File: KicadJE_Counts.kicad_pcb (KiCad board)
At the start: 2 copper layers, 242 x 128 mm, 215 parts, among them J108 Conn_02x03_Male, J201 ClockOut, J202 ClockIn, J203 Out0, J204 Out1, J205 Out2, J206 Out3, J207 Out4, J208 Out5, J209 Out6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

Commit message: Update KicadJE_Counts.kicad_pcb
input circuit
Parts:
- moved R331 103.4 mm to (45.4, 106.1)
- moved C321 97.8 mm to (45.2, 110.0)
- moved R304 76.0 mm to (85.8, 112.0)
- moved R303 72.9 mm to (82.0, 112.0)
- moved R301 67.6 mm to (58.0, 112.0), turned to 180 degrees
- moved R302 64.7 mm to (54.2, 112.0), turned to 180 degrees
- moved D314 56.9 mm to (44.8, 99.5)
- moved D313 56.9 mm to (44.9, 101.8)
- moved D307 44.8 mm to (42.5, 119.2)
- moved D308 44.8 mm to (42.7, 117.1)
- moved C313 7.06 mm to (62.0, 112.0), turned to 180 degrees
- moved C314 6.74 mm to (78.0, 112.0), turned to 0 degrees
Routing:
- net Net-(C314-Pad1): track 0.00 -> 40.0 mm
- net Net-(C313-Pad1): track 0.00 -> 21.0 mm
- net -12V: track 90.7 -> 93.2 mm
- net +12V: track 141.7 -> 144.2 mm
- net Net-(C314-Pad2): track 0.00 -> 2.45 mm
- net Net-(C313-Pad2): track 0.00 -> 1.98 mm
- net In_2: track 0.00 -> 1.70 mm
- net In_1: track 0.00 -> 1.68 mm

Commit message: Update KicadJE_Counts.kicad_pcb
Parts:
- moved R313 126.6 mm to (84.5, 62.5), turned to 180 degrees
- moved C315 116.8 mm to (75.2, 67.8), turned to 270 degrees
- moved R320 112.3 mm to (78.0, 85.0), turned to 180 degrees
- moved R326 111.7 mm to (81.8, 85.0), turned to 180 degrees
- moved R315 111.5 mm to (63.8, 63.2), turned to 270 degrees
- moved R306 111.4 mm to (75.2, 64.0), turned to 90 degrees
- moved R314 110.4 mm to (84.5, 65.0), turned to 180 degrees
- moved R319 104.3 mm to (56.0, 87.5)
- moved R316 104.0 mm to (63.8, 67.0), turned to 270 degrees
- moved D309 96.9 mm to (55.2, 65.0), turned to 270 degrees
- moved D310 94.0 mm to (57.5, 65.0), turned to 90 degrees
- moved R328 86.6 mm to (56.0, 85.0)
- moved R321 76.6 mm to (80.0, 94.0), turned to 180 degrees
- moved D307 64.4 mm to (77.2, 65.0), turned to 90 degrees
- moved D308 63.8 mm to (79.5, 65.0), turned to 270 degrees
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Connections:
- R313 pad 1: (no net) -> /KicadJE_Counts2/POT3_L
- RV303 pad 1: (no net) -> /KicadJE_Counts2/POT3_L

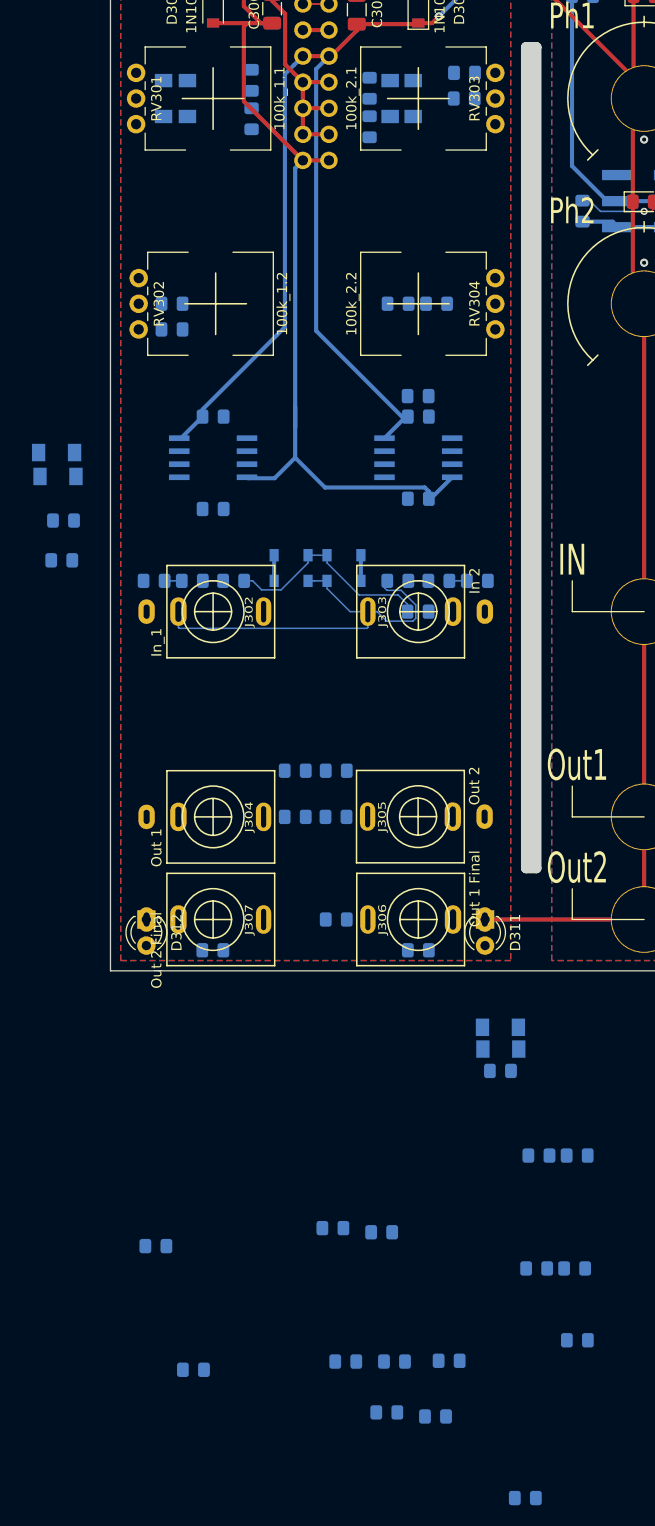
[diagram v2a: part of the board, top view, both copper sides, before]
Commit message: Changed label types for POT's
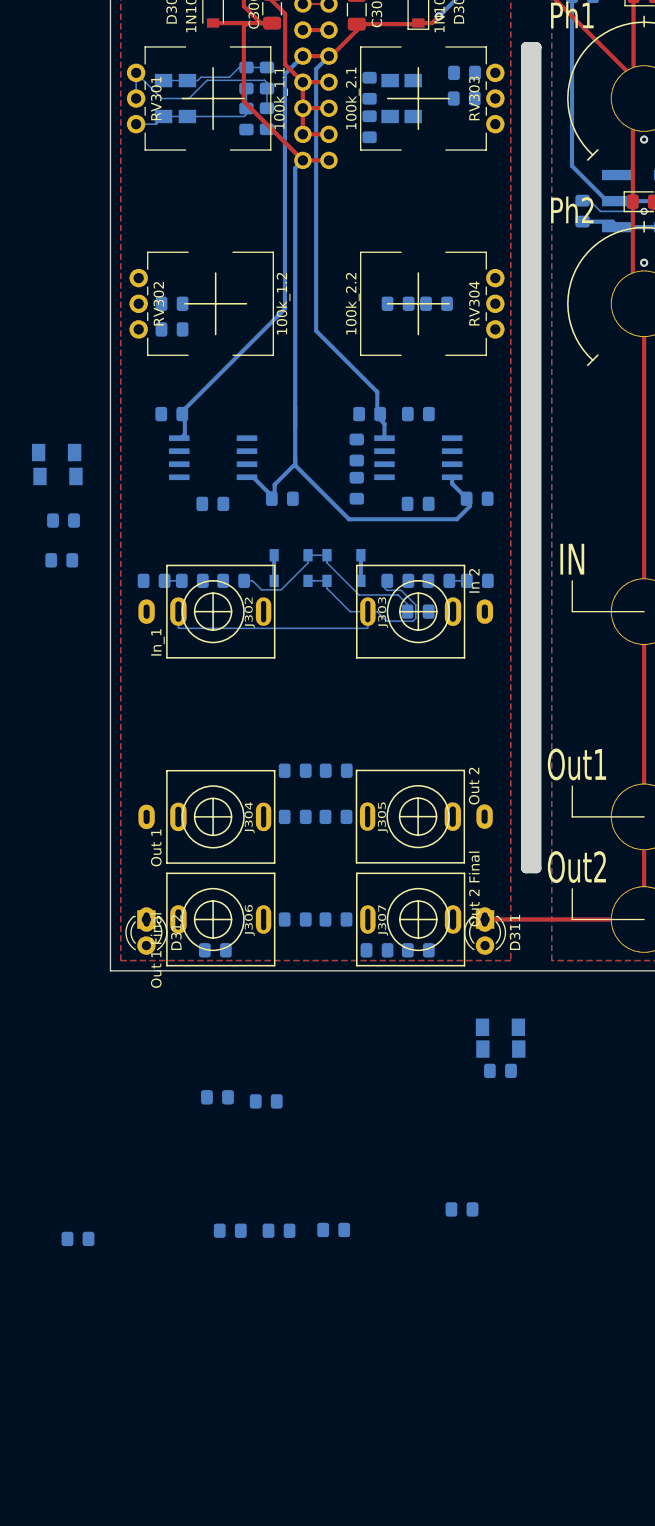
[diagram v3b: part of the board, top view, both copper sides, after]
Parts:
- moved C320 119.4 mm to (63.2, 63.0), turned to 90 degrees
- moved R307 116.5 mm to (63.2, 67.0), turned to 270 degrees
- moved R323 101.5 mm to (60.0, 104.5), turned to 180 degrees
- moved R322 88.9 mm to (80.0, 104.5), turned to 180 degrees
- moved R308 71.0 mm to (74.0, 99.2), turned to 90 degrees
- moved R311 68.5 mm to (74.0, 103.0), turned to 90 degrees
- moved R330 45.0 mm to (76.0, 148.0)
- moved C319 36.3 mm to (72.0, 145.0), turned to 180 degrees
- moved J306 20.0 mm to (60.0, 145.0), turned to 270 degrees
- moved J307 20.0 mm to (80.0, 145.0), turned to 90 degrees
- moved R309 17.0 mm to (71.8, 175.2)
- moved R310 17.0 mm to (46.8, 176.1)
- moved R312 17.0 mm to (84.2, 173.2)
- moved R324 17.0 mm to (65.2, 162.7)
- moved R325 17.0 mm to (66.4, 175.3)
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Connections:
- net /KicadJE_Counts2/POT1_L renamed POT1_L
- R315 pad 2: /KicadJE_Counts2/POT1_C -> POT1_C
- R316 pad 1: /KicadJE_Counts2/POT1_C -> POT1_C
- RV301 pad 2: /KicadJE_Counts2/POT1_C -> POT1_C
- RV301 pad 3: (no net) -> POT1_C
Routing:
- net POT1_C: track 0.00 -> 19.6 mm
- net POT1_L: track 0.00 -> 14.8 mm
- net Net-(C320-Pad2): track 0.00 -> 10.6 mm
- net -12V: track 93.2 -> 101.1 mm
- net +12V: track 144.2 -> 141.9 mm

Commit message: Update KicadJE_Counts.kicad_pcb
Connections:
- net /KicadJE_Counts2/POT2_L renamed POT2_L
- net /KicadJE_Counts2/POT3_L renamed POT3_L
- net /KicadJE_Counts2/POT4_L renamed POT4_L
- R314 pad 1: /KicadJE_Counts2/POT3_C -> POT3_C
- R317 pad 1: /KicadJE_Counts2/POT3_C -> POT3_C
- R322 pad 2: /KicadJE_Counts2/POT3_C -> POT3_C
- R327 pad 2: /KicadJE_Counts2/POT4_C -> POT4_C
- R328 pad 1: /KicadJE_Counts2/POT2_C -> POT2_C
- R330 pad 2: /KicadJE_Counts2/POT4_C -> POT4_C
- RV302 pad 2: /KicadJE_Counts2/POT2_C -> POT2_C
- RV302 pad 3: (no net) -> POT2_C
- RV303 pad 2: /KicadJE_Counts2/POT3_C -> POT3_C
- RV303 pad 3: (no net) -> POT3_C
- RV304 pad 2: /KicadJE_Counts2/POT4_C -> POT4_C
- RV304 pad 3: (no net) -> POT4_C
- U301 pad 1: /KicadJE_Counts2/POT4_C -> POT4_C
- U301 pad 7: /KicadJE_Counts2/POT3_C -> POT3_C
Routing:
- net POT4_C: track 0.00 -> 16.3 mm
- net POT2_C: track 0.00 -> 5.92 mm
- net POT4_L: track 0.00 -> 5.74 mm
- net POT2_L: track 0.00 -> 2.23 mm
- net Net-(R320-Pad1): track 0.00 -> 1.70 mm

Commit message: Update KicadJE_Counts.kicad_pcb
components placed
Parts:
- removed the H301 at (2.53, 183.5)
- removed H303: 2,5mm, MountingHole:MountingHole_2.5mm_Pad_Via
- moved R325 75.6 mm to (66.8, 99.8), turned to 180 degrees
- moved R312 75.4 mm to (53.2, 104.5), turned to 0 degrees
- moved R310 68.7 mm to (53.2, 107.8), turned to 180 degrees
- moved R309 68.3 mm to (82.0, 107.8)
- moved H302 68.2 mm to (43.0, 130.0)
- moved H304 66.2 mm to (43.5, 122.0)
- moved R324 65.6 mm to (86.8, 100.8), turned to 180 degrees
- moved D314 56.1 mm to (79.5, 143.5)
- moved D313 56.0 mm to (79.5, 145.8)
- moved C321 46.6 mm to (80.0, 141.0)
- moved R331 43.4 mm to (72.0, 140.5), turned to 180 degrees
- moved R333 35.4 mm to (68.0, 140.5)
- moved C322 34.0 mm to (60.0, 140.5)
- moved D315 29.9 mm to (60.8, 143.2)
- moved D316 29.9 mm to (60.8, 145.4)
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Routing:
- net Out1_Final: track 0.00 -> 13.9 mm
- net Net-(C321-Pad1): track 0.00 -> 12.0 mm
- net Net-(C322-Pad1): track 0.00 -> 11.8 mm
- net Net-(C315-Pad1): track 0.00 -> 11.7 mm
- net Net-(R328-Pad2): track 0.00 -> 11.0 mm
- net Net-(R321-Pad1): track 0.00 -> 10.7 mm
- net Net-(C315-Pad2): track 0.00 -> 10.6 mm
- net Out2_Final: track 0.00 -> 10.2 mm
- net Net-(R323-Pad1): track 0.00 -> 8.69 mm
- net Net-(R310-Pad1): track 0.00 -> 7.19 mm
- net Net-(R320-Pad1): track 1.70 -> 8.46 mm
- net POT3_C: track 0.00 -> 6.41 mm
- net Net-(D312-Pad2): track 0.00 -> 5.89 mm
- net In_1: track 1.68 -> 7.53 mm
- net -12V: track 101.1 -> 106.9 mm
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
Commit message: Update KicadJE_Counts.kicad_pcb
wired
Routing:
- net POT3_C: track 6.41 -> 86.4 mm, vias 0 -> 2
- net Net-(R316-Pad2): track 0.00 -> 79.0 mm
- net Net-(R328-Pad2): track 11.0 -> 84.0 mm, vias 0 -> 4
- net Net-(C315-Pad1): track 11.7 -> 79.3 mm
- net POT4_C: track 18.2 -> 76.1 mm
- net POT1_L: track 14.8 -> 52.2 mm
- net POT2_L: track 2.23 -> 23.9 mm
- net Net-(R320-Pad1): track 8.46 -> 26.0 mm, vias 0 -> 2
- net +12V: track 147.3 -> 162.9 mm, vias 1 -> 3
- net GND: track 201.9 -> 216.4 mm, vias 5 -> 25
- net Net-(C313-Pad1): track 21.0 -> 25.3 mm
- net Net-(J303-PadTN): track 0.00 -> 2.38 mm
- net Net-(C317-Pad1): track 0.00 -> 2.07 mm
- net Net-(C316-Pad1): track 0.00 -> 2.05 mm

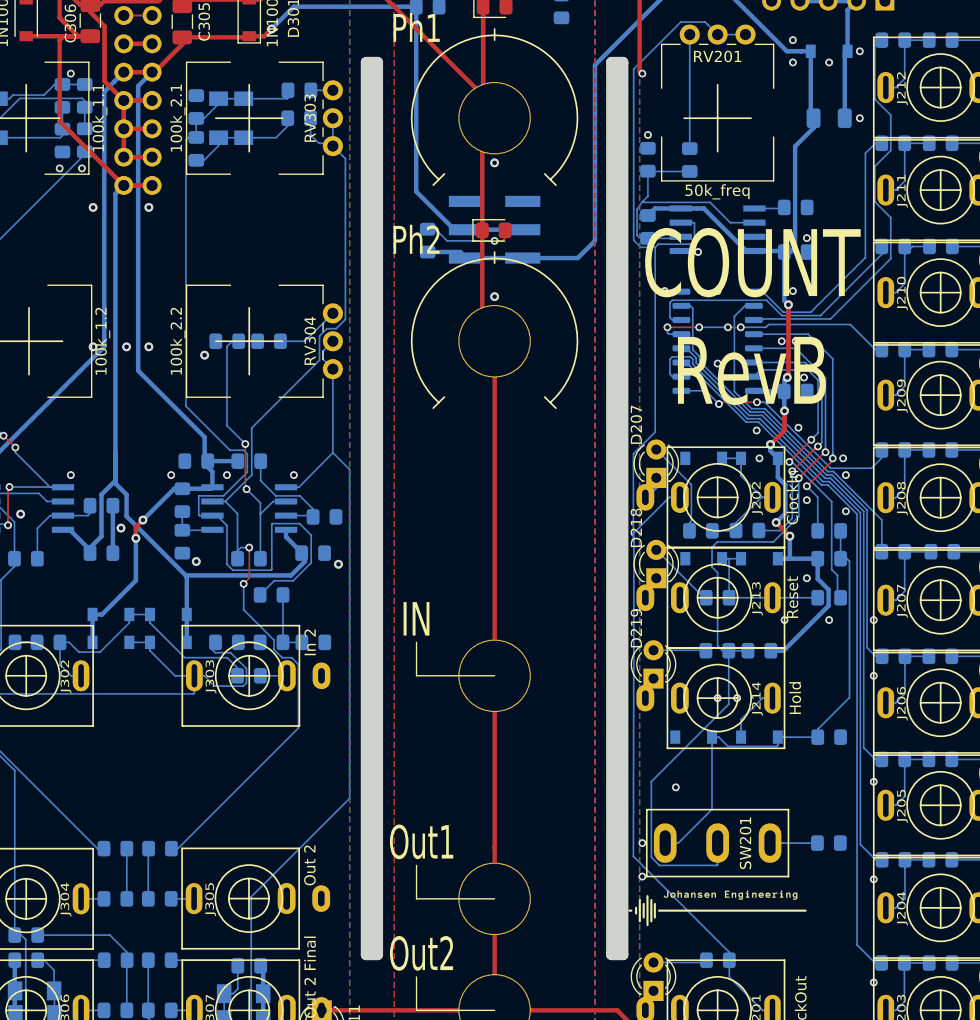
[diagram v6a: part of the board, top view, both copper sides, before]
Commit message: Update KicadJE_Counts.kicad_pcb
DRC
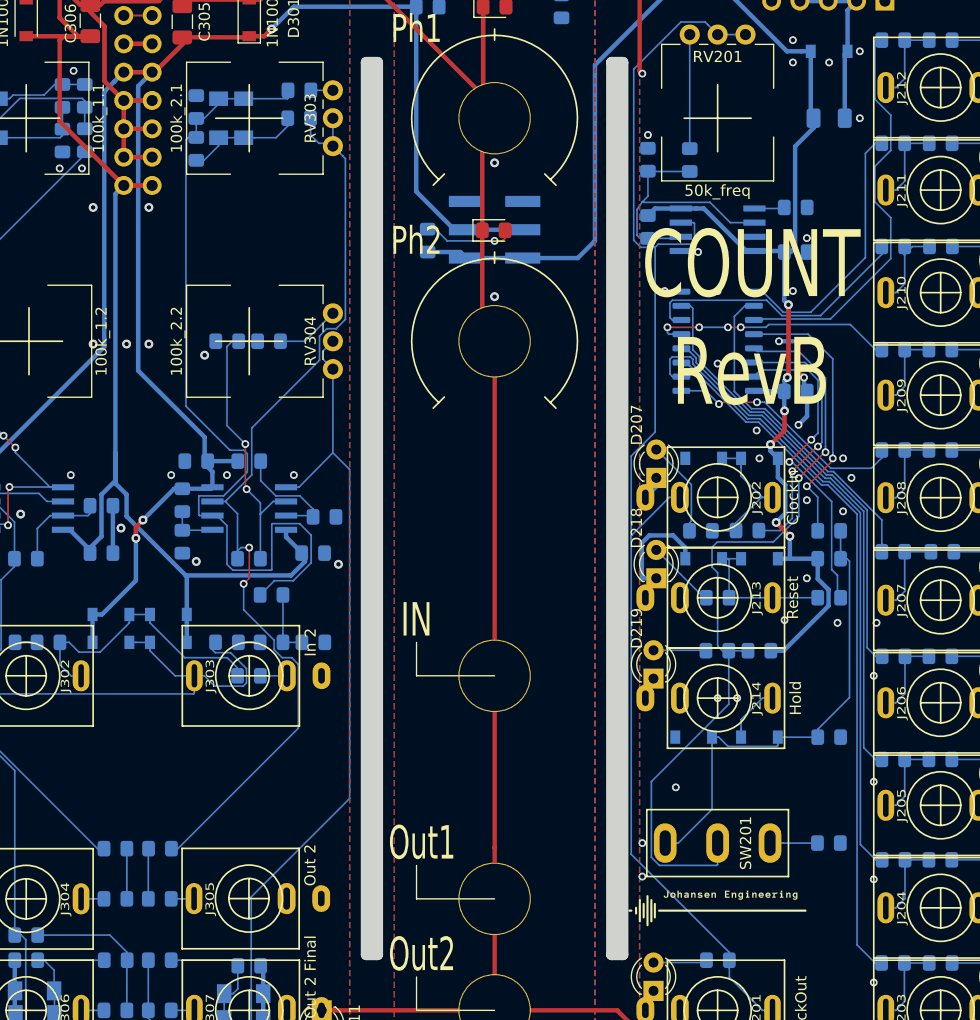
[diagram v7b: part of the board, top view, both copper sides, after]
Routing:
- net GNDS: track 77.9 -> 97.9 mm
- net Out7: track 7.18 -> 8.05 mm
